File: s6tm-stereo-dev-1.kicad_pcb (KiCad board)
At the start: 4 copper layers, 85 x 80 mm, 190 parts, among them J1 Micro_SD_Card_Det1, J2 Conn_01x04_Pin, J3 USB_C_Receptacle_USB2.0_14P, J4 Conn_01x02, J5 AudioJack4, J6 Conn_01x02, J7 Conn_01x02, J8 Conn_01x02, Q1 Q_NMOS, Q2 Q_NMOS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

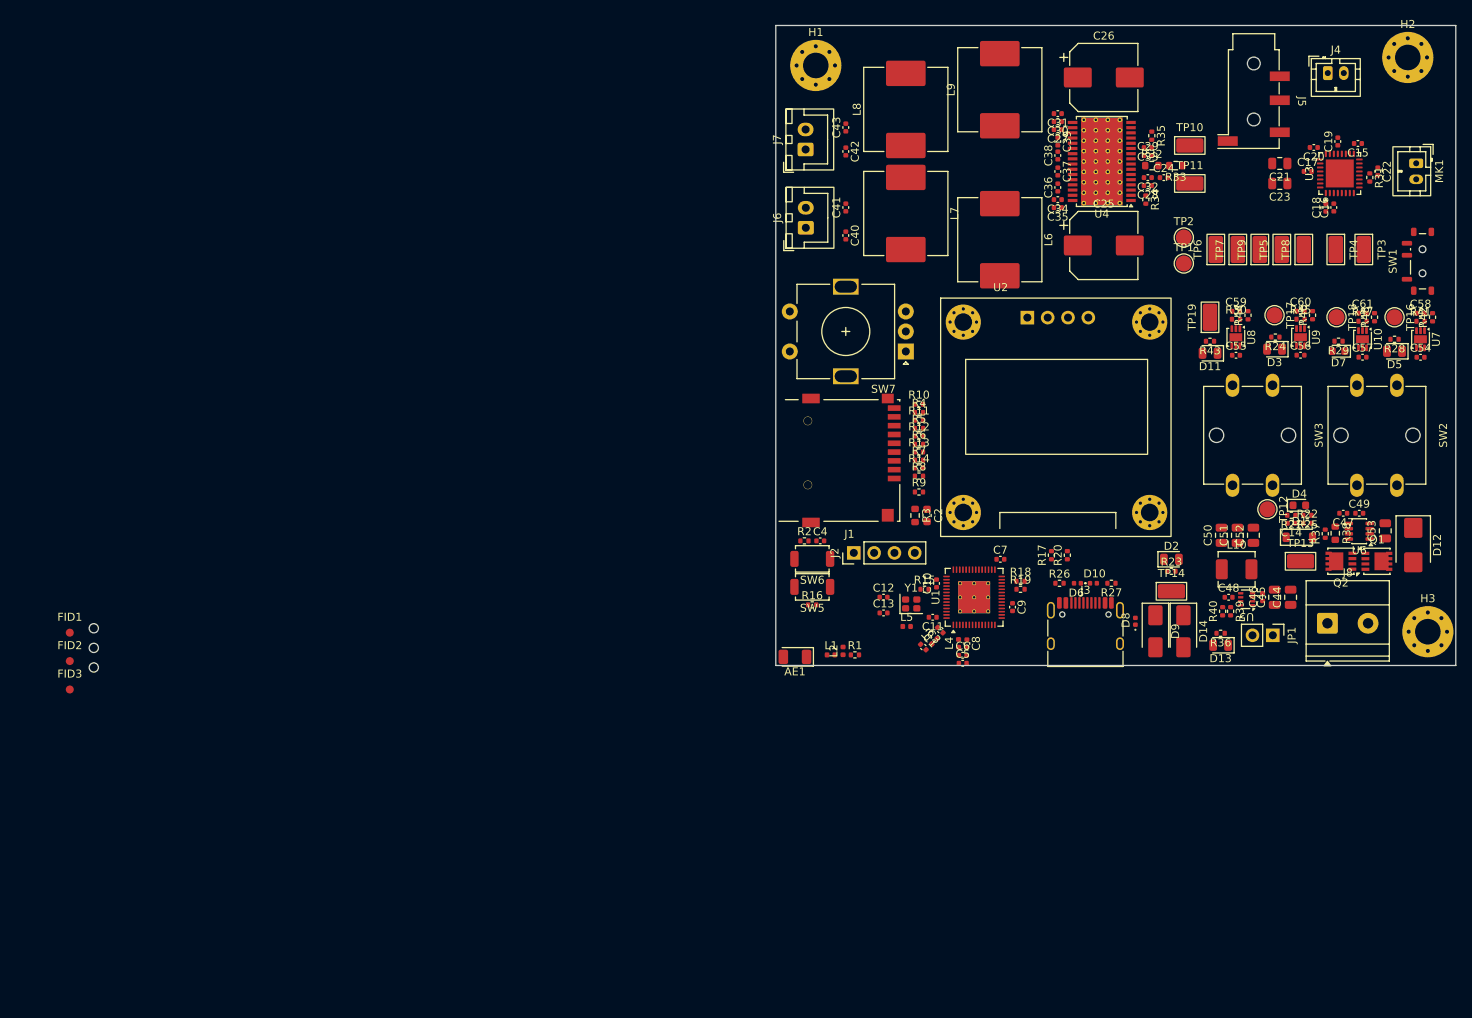
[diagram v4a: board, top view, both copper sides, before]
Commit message: pcb: add fiducials, tooling holes
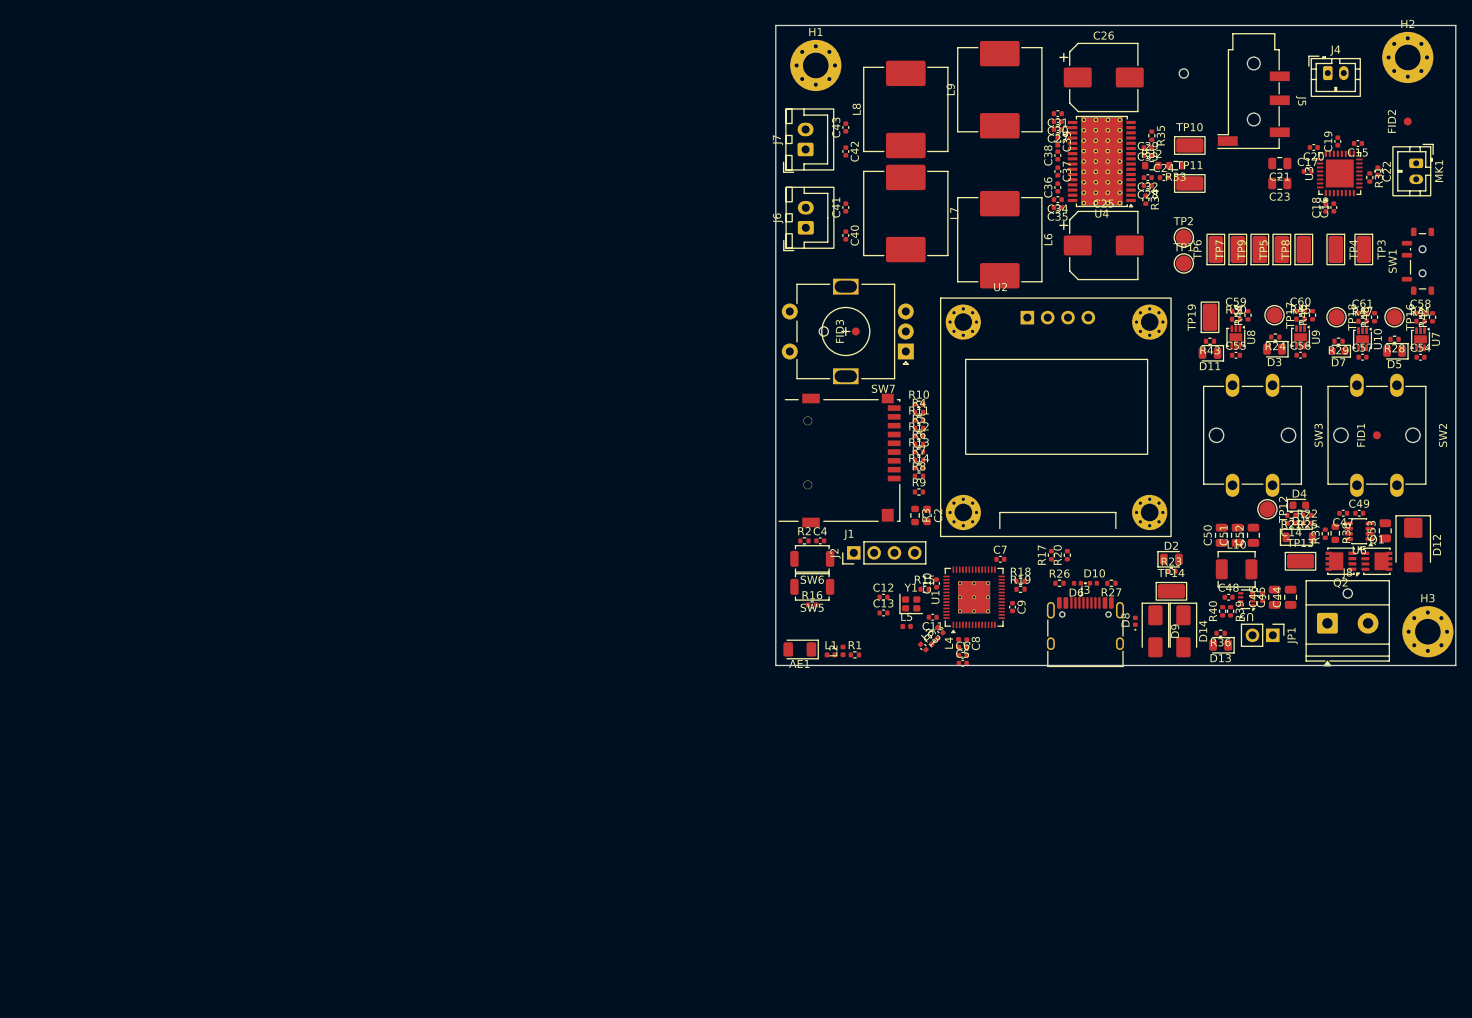
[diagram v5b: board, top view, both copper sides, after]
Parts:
- moved FID2 180.3 mm to (196.0, 79.0), turned to 90 degrees
- moved FID1 165.2 mm to (192.1, 118.2), turned to 90 degrees
- moved H7 157.0 mm to (188.5, 138.0), turned to 90 degrees
- moved H5 152.9 mm to (168.0, 73.0), turned to 90 degrees
- moved FID3 108.0 mm to (127.0, 105.2), turned to 90 degrees
- moved H6 99.5 mm to (123.0, 105.2), turned to 90 degrees
- moved AE1 1.11 mm to (120.0, 145.0)

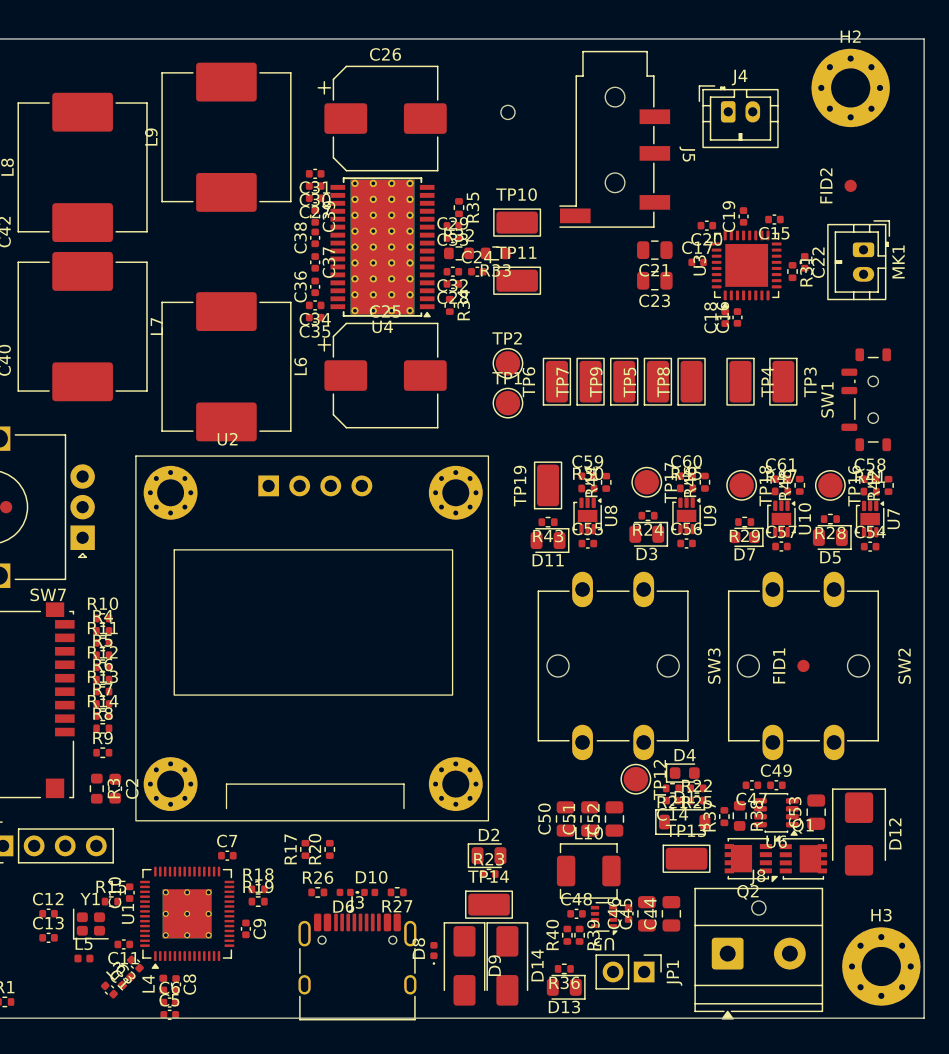
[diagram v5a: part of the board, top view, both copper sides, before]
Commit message: pcb: refine sd layout
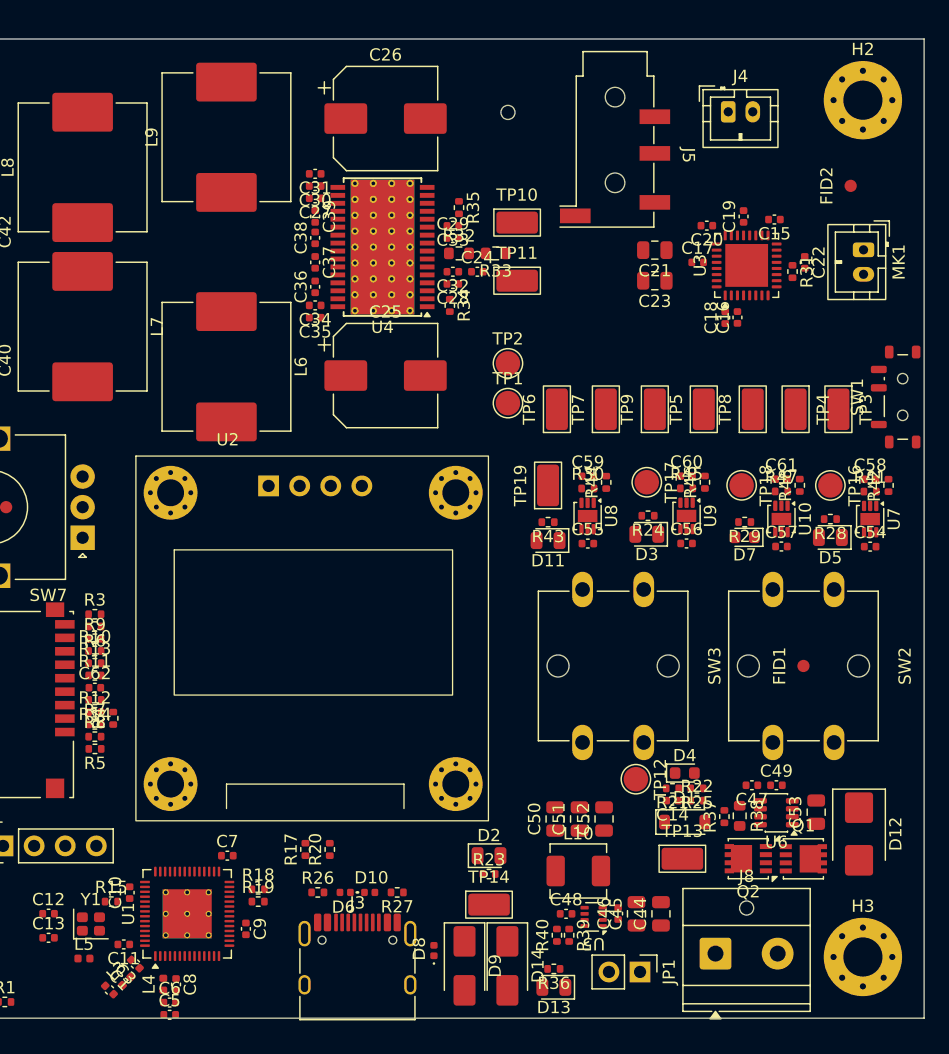
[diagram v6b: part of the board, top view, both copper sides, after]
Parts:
- removed C2: 0u1, Capacitor_SMD:C_0603_1608Metric
- added C62: 1u, Capacitor_SMD:C_0402_1005Metric, F.Cu at (134.2, 120.0)
- R3: footprint Resistor_SMD:R_0603_1608Metric -> Resistor_SMD:R_0402_1005Metric
- moved R3 14.3 mm to (134.2, 114.0), turned to 0 degrees
- moved R9 9.34 mm to (134.2, 116.0)
- moved R5 7.67 mm to (134.3, 125.0), turned to 180 degrees
- moved R4 7.19 mm to (135.8, 122.5), turned to 90 degrees
- moved TP8 5.48 mm to (188.0, 97.2)
- moved TP3 5.03 mm to (195.0, 97.2)
- moved TP4 5.03 mm to (191.5, 97.2)
- moved R6 4.39 mm to (134.2, 115.0), turned to 180 degrees
- moved TP5 4.37 mm to (184.0, 97.2)
- moved R12 3.73 mm to (134.2, 122.0)
- moved TP9 3.36 mm to (180.0, 97.2)
- moved R11 2.74 mm to (134.2, 119.0)
- moved R10 2.73 mm to (134.2, 117.0)
- moved TP7 2.57 mm to (176.0, 97.2)
- moved SW1 2.42 mm to (200.2, 96.2)
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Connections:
- R3 pad 1: +3V3 -> Net-(J1-DET)
- R3 pad 2: Net-(J1-DET) -> +3V3

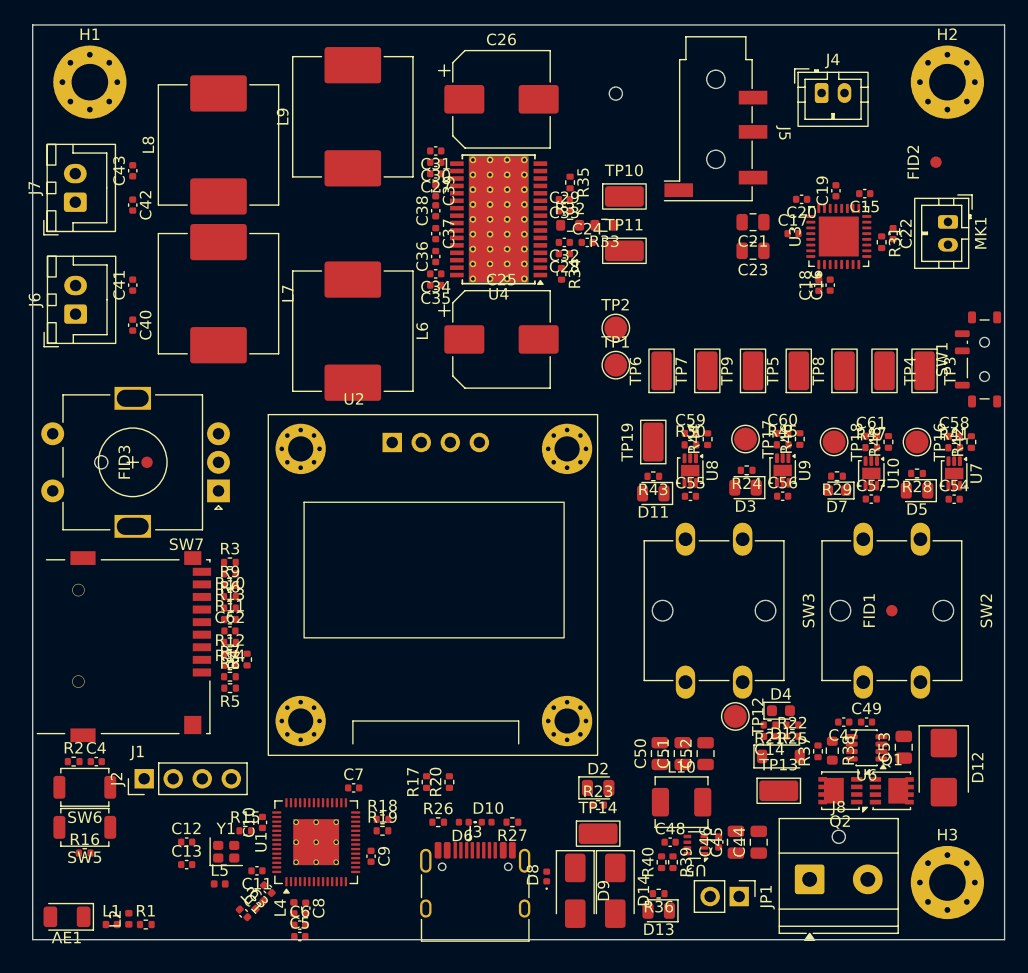
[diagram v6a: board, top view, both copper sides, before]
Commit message: pcb: add board outline
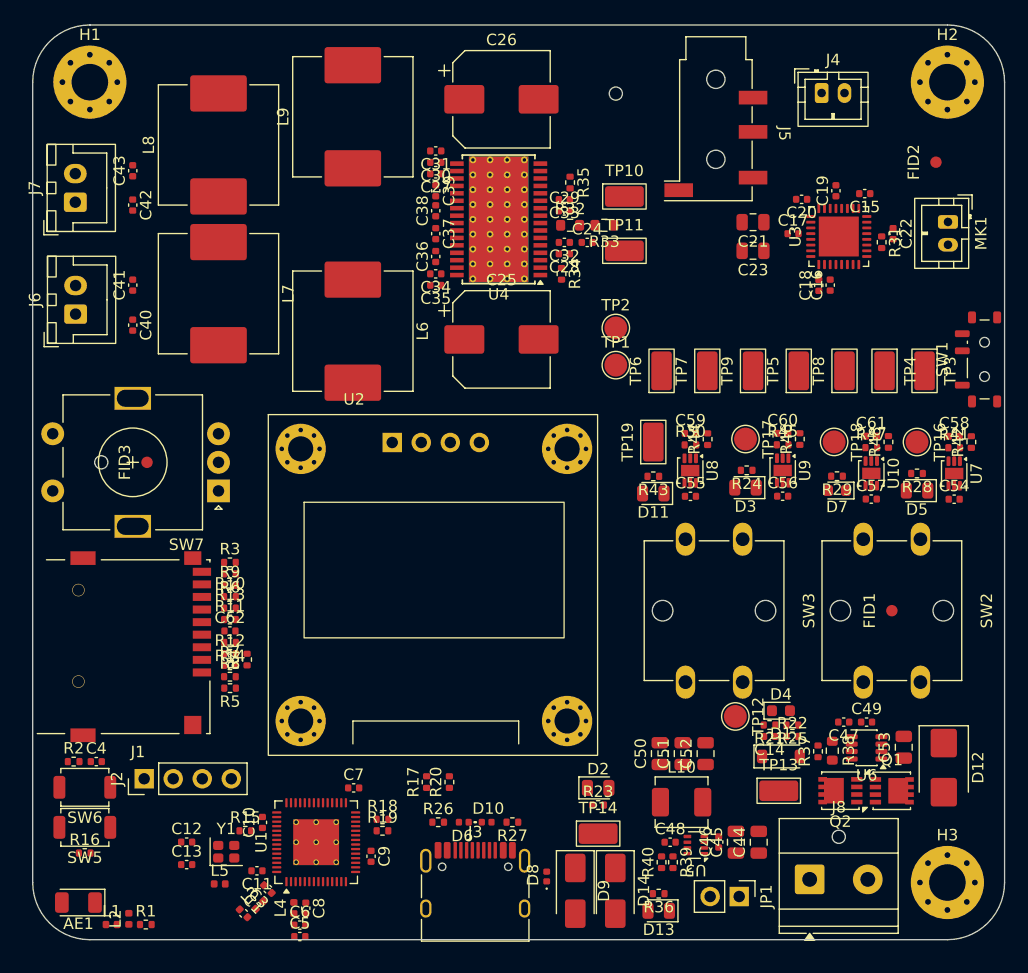
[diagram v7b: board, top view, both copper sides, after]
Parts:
- moved AE1 1.60 mm to (121.0, 143.8)
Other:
- outline, holes or cut-outs redrawn
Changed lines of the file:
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@@
 	(footprint "RF_Antenna:Johanson_2450AT18x100"
 		(layer "F.Cu")
-		(at 120 145 180)
+		(at 121 143.75 180)
 		(descr "Johanson 2450AT43F0100 SMD antenna 2400-2500Mhz, -0.5dBi, https://www.johansontechnology.com/datasheets/2450AT18A100/2450AT18A100.pdf")
 		(tags "antenna")
@@
 		)
 	)
-	(gr_rect
-		(start 117 67)
-		(end 202 147)
+	(gr_arc
+		(start 117 72)
+		(mid 118.464466 68.464466)
+		(end 122 67)
+		(stroke
+			(width 0.05)
+			(type default)
+		)
+		(layer "Edge.Cuts")
+	)
+	(gr_line
+		(start 117 142)
+		(end 117 72)
+		(stroke
+			(width 0.05)
+			(type default)
+		)
+		(layer "Edge.Cuts")
+	)
+	(gr_line
+		(start 122 67)
+		(end 197 67)
+		(stroke
+			(width 0.05)
+			(type default)
+		)
+		(layer "Edge.Cuts")
+	)
+	(gr_arc
+		(start 122 147)
+		(mid 118.464466 145.535534)
+		(end 117 142)
+		(stroke
+			(width 0.05)
+			(type default)
+		)
+		(layer "Edge.Cuts")
+	)
+	(gr_arc
+		(start 197 67)
+		(mid 200.535534 68.464466)
+		(end 202 72)
+		(stroke
+			(width 0.05)
+			(type default)
+		)
+		(layer "Edge.Cuts")
+	)
+	(gr_line
+		(start 197 147)
+		(end 122 147)
+		(stroke
+			(width 0.05)
+			(type default)
+		)
+		(layer "Edge.Cuts")
+	)
+	(gr_line
+		(start 202 72)
+		(end 202 142)
+		(stroke
+			(width 0.05)
+			(type default)
+		)
+		(layer "Edge.Cuts")
+	)
+	(gr_arc
+		(start 202 142)
+		(mid 200.535534 145.535534)
+		(end 197 147)
 		(stroke
 			(width 0.05)
 			(type default)
 		)
-		(fill no)
 		(layer "Edge.Cuts")
 	)
